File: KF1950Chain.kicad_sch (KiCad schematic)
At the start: 74 parts, among them Q2 MMBT3906, U11 TXS0101DRL, U12 SPX3819M5-L-1-8, U22 SPX3819M5-L-1-8, U6 SPX3819M5-L-1-8, Y1 ASE-24MHz

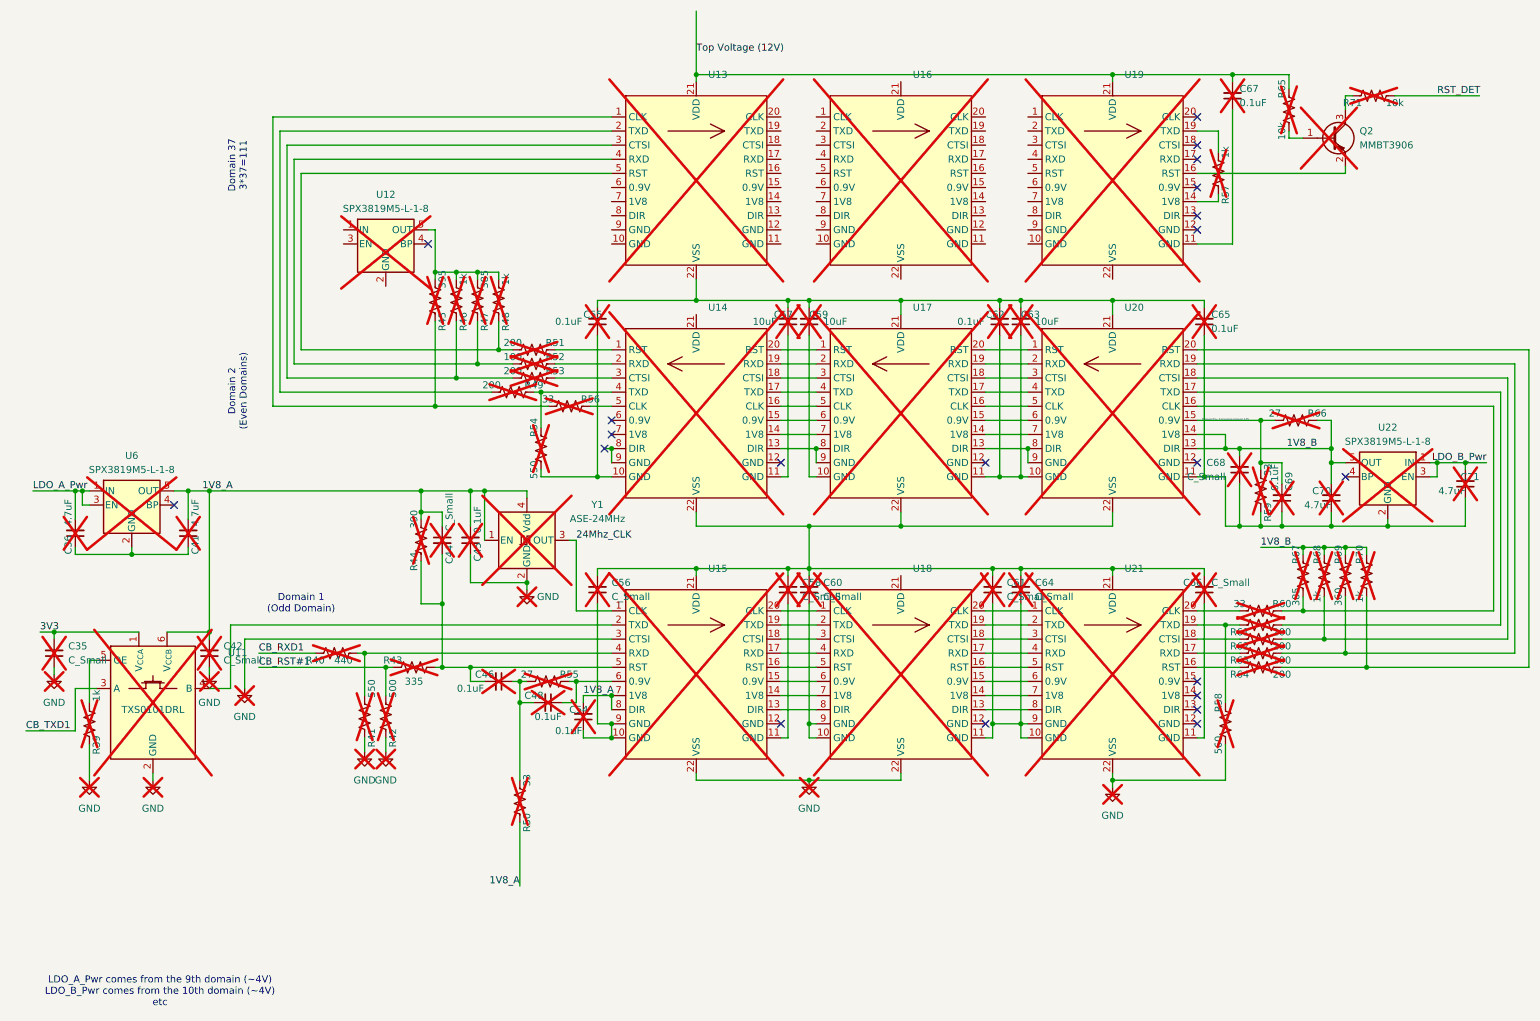
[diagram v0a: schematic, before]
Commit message: All components placed
Went through TI schematic and layout checklist.
All components placed and initial DRC
Need thermal vias on KF1950 and also better layout (so not so many errors)
Need to do silk
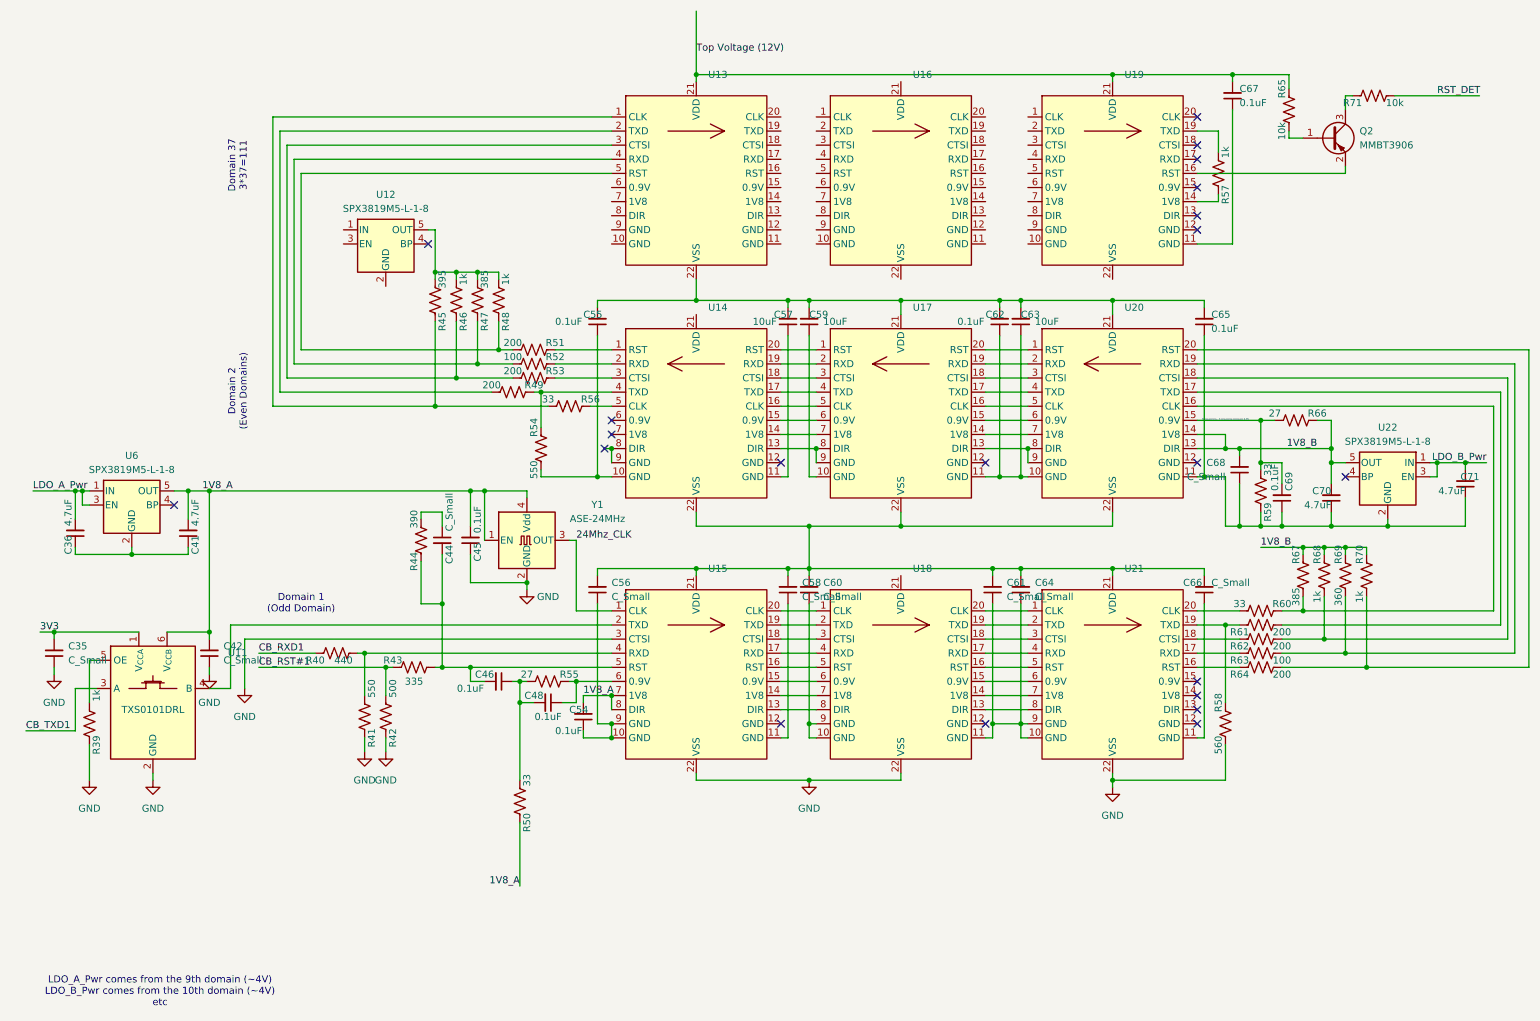
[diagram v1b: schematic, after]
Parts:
- C35, C36, C41, C42, C44, C45, C46, C48, C54, C55, C56, C57, C58, C59, C60, C61, C62, C63, C64, C65, C66, C67, C68, C69, C70, C71, Q2, R39, R40, R41, R42, R43, R44, R45, R46, R47, R48, R49, R50, R51, R52, R53, R54, R55, R56, R57, R58, R59, R60, R61, R62, R63, R64, R65, R66, R67, R68, R69, R70, R71, U11, U12, U13, U14, U15, U16, U17, U18, U19, U20, U21, U22, U6, Y1: now fitted
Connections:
- net 1V8_A: no longer C44.1, R44.2
- new net: C44.1, R44.2
